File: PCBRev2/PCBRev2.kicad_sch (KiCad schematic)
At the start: 55 parts, among them J1 Conn_02x40_Counter_Clockwise, J3 512964594, J5 Keypad, J6 Conn_02x10_Odd_Even, J7 54-00164, Q1 2N7000, SW1 SW_Push, SW2 SW_Push, SW3 SW_Push, U1 NUCLEO-G0B1RE, U10 BH1750FVI-TR, U11 MCP6002-I_P, U12 DRV8833PWP, U2 LP-MSPM0G3507, U4 SN74AHC14N, U5 LM7805_TO220, U6 TLV1117-33, U7 COM-09032, U8 WST-1205S, U9 AL5809-20QP1-7

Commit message: Routing for second revision of the PCB
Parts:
- removed C_BP3, C_BP4: 100 uf, Capacitor_THT:C_Axial_L3.8mm_D2.6mm_P7.50mm_Horizontal, symbol Device:C_Small
- removed D1: ASMB-MTB1-0A3A2, LED_SMD:LED_Avago_PLCC4_3.2x2.8mm_CW, symbol LED:ASMB-MTB1-0A3A2
- removed J1: Conn_02x40_Counter_Clockwise, Connector_PinHeader_2.54mm:PinHeader_2x40_P2.54mm_Vertical, symbol Connector_Generic:Conn_02x40_Counter_Clockwise
- removed R_BUZ2: 100kR, Resistor_THT:R_Axial_DIN0207_L6.3mm_D2.5mm_P5.08mm_Vertical, symbol Device:R
- removed U8: WST-1205S, WST-1205S.step:WST-1205S, symbol WST-1205S:WST-1205S
- added C10: 0.22uf, GRM155R71C224KA12D022uf.step:CAPC1005X55N, symbol Device:C_Small
- added C11: 1uf, CL03A105KP3NSNC1uf.step:CAPC0603X35N, symbol Device:C_Small
- added D2: AAAF3529LSEEZGKQBKS, LED_AAAF3529LSEEZGKQBKS_KNB, symbol 2025-11-19_19-46-32:AAAF3529LSEEZGKQBKS
- added D3, D4, D5: LED, LED_THT:LED_D3.0mm_FlatTop, symbol Device:LED
- added J6: Conn_02x30_Odd_Even, Connector_PinHeader_2.54mm:PinHeader_2x30_P2.54mm_Vertical, symbol Connector_Generic:Conn_02x30_Odd_Even
- added R19, R20: 68, CRGCQ1206F68R.step:RESC3115X65N, symbol Device:R
- added R21: 330, CRCW1210330RFKEAHP.step:RESC3225X70N, symbol Device:R
- added U9: WST-1205S, WST-1205S.step:WST-1205S, symbol WST-1205S:WST-1205S
- C1: renamed from C_BP1; value 0.1 uf -> 0.1uf; footprint Capacitor_THT:C_Axial_L3.8mm_D2.6mm_P7.50mm_Horizontal -> C01UF.step:CAPC1608X90
- C2: renamed from C_BP2; value 47 uf -> 47uf; footprint Capacitor_THT:C_Radial_D10.0mm_H20.0mm_P5.00mm -> GRM32EC81C476KE15L.step:CAPC3225X270N
- C3: renamed from CSW1; footprint Capacitor_THT:C_Axial_L3.8mm_D2.6mm_P7.50mm_Horizontal -> GRM033R60J474KE90D.step:CAPC0603X33N
- C4: renamed from CSW3; footprint Capacitor_THT:C_Axial_L3.8mm_D2.6mm_P7.50mm_Horizontal -> GRM033R60J474KE90D.step:CAPC0603X33N
- C5: renamed from CJS1; footprint Capacitor_THT:C_Axial_L3.8mm_D2.6mm_P7.50mm_Horizontal -> GRM033R60J474KE90D.step:CAPC0603X33N
- C6: renamed from C_s2; footprint Capacitor_THT:C_Axial_L3.8mm_D2.6mm_P7.50mm_Horizontal -> CL03A105KP3NSNC1uf.step:CAPC0603X35N
- Q1: value 2N7000 -> 2N4401
- R1: renamed from PullUpResistorSW1; footprint Resistor_THT:R_Axial_DIN0207_L6.3mm_D2.5mm_P5.08mm_Vertical -> RC0603FR_0710KL.step:RESC1607X60N
- R10: renamed from R_SNSA2; footprint Resistor_THT:R_Axial_DIN0207_L6.3mm_D2.5mm_P5.08mm_Vertical -> CRGCQ0603F2K2.step:RESC1608X55N
- R11: renamed from R_SNSA3; footprint Resistor_THT:R_Axial_DIN0207_L6.3mm_D2.5mm_P5.08mm_Vertical -> CRGCQ0603F2K2.step:RESC1608X55N
- R12: renamed from R_SNSA5; footprint Resistor_THT:R_Axial_DIN0207_L6.3mm_D2.5mm_P5.08mm_Vertical -> CRGCQ0603F2K2.step:RESC1608X55N
- R13: renamed from R_SNSA6; footprint Resistor_THT:R_Axial_DIN0207_L6.3mm_D2.5mm_P5.08mm_Vertical -> CRGCQ0603F2K2.step:RESC1608X55N
- R14: renamed from R_SNSA4; value 70kR -> 68k; footprint Resistor_THT:R_Axial_DIN0207_L6.3mm_D2.5mm_P5.08mm_Vertical -> CRGP2512F68K.step:RESC6332X65N
- R15: renamed from R_BUZ1; value 100R -> 1kR
- R16: renamed from PullUpResistor2; footprint Resistor_THT:R_Axial_DIN0207_L6.3mm_D2.5mm_P5.08mm_Vertical -> RC0603FR_0710KL.step:RESC1607X60N
- R18: renamed from R_INDC1; value 5.5k ohm -> 510; footprint Resistor_THT:R_Axial_DIN0207_L6.3mm_D2.5mm_P5.08mm_Vertical -> RMCF0805JT510R510.step:RESC2012X65N
- R2: renamed from RSW1; footprint Resistor_THT:R_Axial_DIN0207_L6.3mm_D2.5mm_P5.08mm_Vertical -> RC0603FR_0710KL.step:RESC1607X60N
- R3: renamed from PullUpResistorSW3; footprint Resistor_THT:R_Axial_DIN0207_L6.3mm_D2.5mm_P5.08mm_Vertical -> RC0603FR_0710KL.step:RESC1607X60N
- R4: renamed from RSW3; footprint Resistor_THT:R_Axial_DIN0207_L6.3mm_D2.5mm_P5.08mm_Vertical -> RC0603FR_0710KL.step:RESC1607X60N
- R5: renamed from PullUpResistorJS1; footprint Resistor_THT:R_Axial_DIN0207_L6.3mm_D2.5mm_P5.08mm_Vertical -> RC0603FR_0710KL.step:RESC1607X60N
- R6: renamed from RJS1; footprint Resistor_THT:R_Axial_DIN0207_L6.3mm_D2.5mm_P5.08mm_Vertical -> RC0603FR_0710KL.step:RESC1607X60N
- R7: renamed from R_COFF2; footprint Resistor_THT:R_Axial_DIN0207_L6.3mm_D2.5mm_P5.08mm_Vertical -> RNCP1206FTD1K00.step:RESC3216X90N
- R8: renamed from R_COFF3; footprint Resistor_THT:R_Axial_DIN0207_L6.3mm_D2.5mm_P5.08mm_Vertical -> RNCP1206FTD1K00.step:RESC3216X90N
- R9: renamed from R_COFF4; footprint Resistor_THT:R_Axial_DIN0207_L6.3mm_D2.5mm_P5.08mm_Vertical -> RNCP1206FTD1K00.step:RESC3216X90N
- U7: renamed from U4; footprint Schmitt:DIP794W45P254L1969H508Q14 -> SN74AHCT14QDRG4Q1.step:SOIC127P600X175-14N
- renumbered C3 to C7, C2 to C8, C1 to C9, D2 to D1, J7 to J1, J6 to J2, J10 to J3, J5 to J4, J4 to J5, J3 to J8, R10 to R17, SW3 to SW2, SW2 to SW3, U9 to U10, U5 to U2, U6 to U3, U2 to U4, U7 to U5, U12 to U6, U10 to U8
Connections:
- net +12V: now also C10.1
- net +5V: now also U9.+; no longer Q1.3 (D)
- net BuzzerGPIO: now also J6.10 (Pin_10), J6.9 (Pin_9)
- net GNDREF: now also Q1.1 (S), C10.2, C11.2, D2.1, D2.2, D2.3, D3.1 (K), D4.1 (K), D5.1 (K)
- net MicOut: now also J6.27 (Pin_27), J6.28 (Pin_28)
- net MotorControl1: now also J6.1 (Pin_1), J6.2 (Pin_2)
- net MotorControl2: now also J6.5 (Pin_5), J6.6 (Pin_6)
- net Motor_Sleep: now also J6.3 (Pin_3), J6.4 (Pin_4)
- net VDD: now also C11.1
- net G: now reaches R8.1
- net G: now also J6.39 (Pin_39), J6.40 (Pin_40)
- net at R8.2: now also D2.5
- net B: now reaches R7.1
- net B: now also J6.37 (Pin_37), J6.38 (Pin_38)
- net at R7.2: now also D2.4
- net H: now reaches U5.H2 (H)
- net H: now also J6.23 (Pin_23), J6.24 (Pin_24)
- net V: now reaches U5.V2 (V)
- net V: now also J6.21 (Pin_21), J6.22 (Pin_22)
- net SDA: now reaches U8.4 (SDA)
- net SDA: now also J6.31 (Pin_31), J6.32 (Pin_32)
- net SCLlight: now reaches U8.6 (SCL)
- net SCLlight: now also J6.33 (Pin_33), J6.34 (Pin_34)
- net SW1: now reaches U7.2 (1Y)
- net SW1: now also J6.13 (Pin_13), J6.14 (Pin_14), R19.1
- net SW2: now reaches U7.4 (2Y)
- net SW2: now also J6.15 (Pin_15), J6.16 (Pin_16), R20.1
- net JSB: now reaches U7.6 (3Y)
- net JSB: now also J6.17 (Pin_17), J6.18 (Pin_18), R21.1
- net SDO: now reaches J8.29
- net SDO: now also J6.51 (Pin_51), J6.52 (Pin_52)
- net SDI: now reaches J8.30
- net SDI: now also J6.53 (Pin_53), J6.54 (Pin_54)
- net SCL: now reaches J8.32
- net SCL: now also J6.55 (Pin_55), J6.56 (Pin_56)
- net D/CX: now reaches J8.33
- net D/CX: now also J6.57 (Pin_57), J6.58 (Pin_58)
- net CSX: now reaches J8.34
- net CSX: now also J6.59 (Pin_59), J6.60 (Pin_60)
- net RESX: now reaches J8.6
- net RESX: now also J6.49 (Pin_49), J6.50 (Pin_50)
- net R: now reaches R9.1
- net R: now also J6.41 (Pin_41), J6.42 (Pin_42)
- net at R9.2: now also D2.6
- net Button No Debouning renamed ButtonNoDebounce
- net ButtonNoDebounce: now also J6.45 (Pin_45), J6.46 (Pin_46)
- new net: D3.2 (A), R19.2
- new net: J6.11 (Pin_11), J6.12 (Pin_12)
- new net: J6.19 (Pin_19), J6.20 (Pin_20)
- new net: J6.25 (Pin_25), J6.26 (Pin_26)
- new net: J6.29 (Pin_29), J6.30 (Pin_30)
- new net: J6.35 (Pin_35), J6.36 (Pin_36)
- new net: J6.43 (Pin_43), J6.44 (Pin_44)
- new net: J6.47 (Pin_47), J6.48 (Pin_48)
- new net: J6.7 (Pin_7), J6.8 (Pin_8)
- new net: Q1.3 (D), U9.-
- new net: D4.2 (A), R20.2
- new net: D5.2 (A), R21.2
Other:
- moved on the sheet: R16, R7, R8, R9, SW3, U8

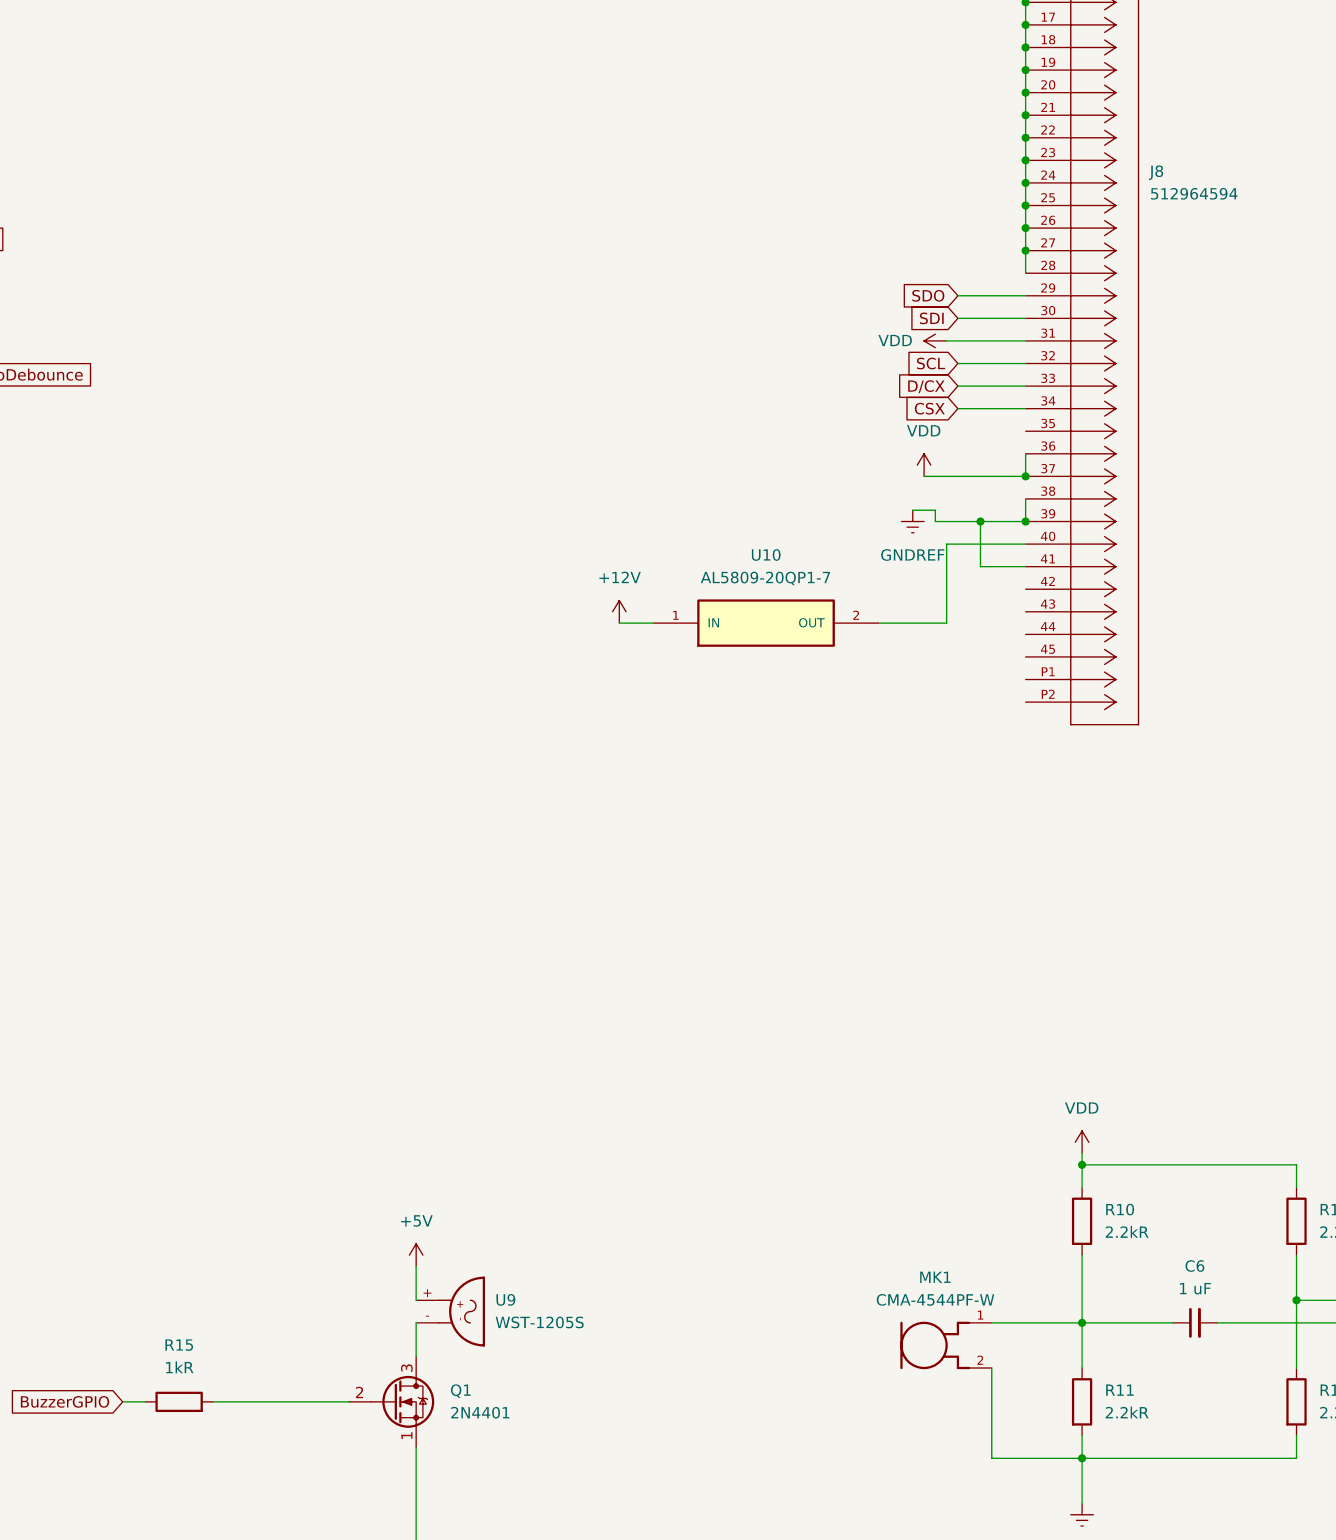
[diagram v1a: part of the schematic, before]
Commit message: Updated routing and footprints for 2nd PCB revision
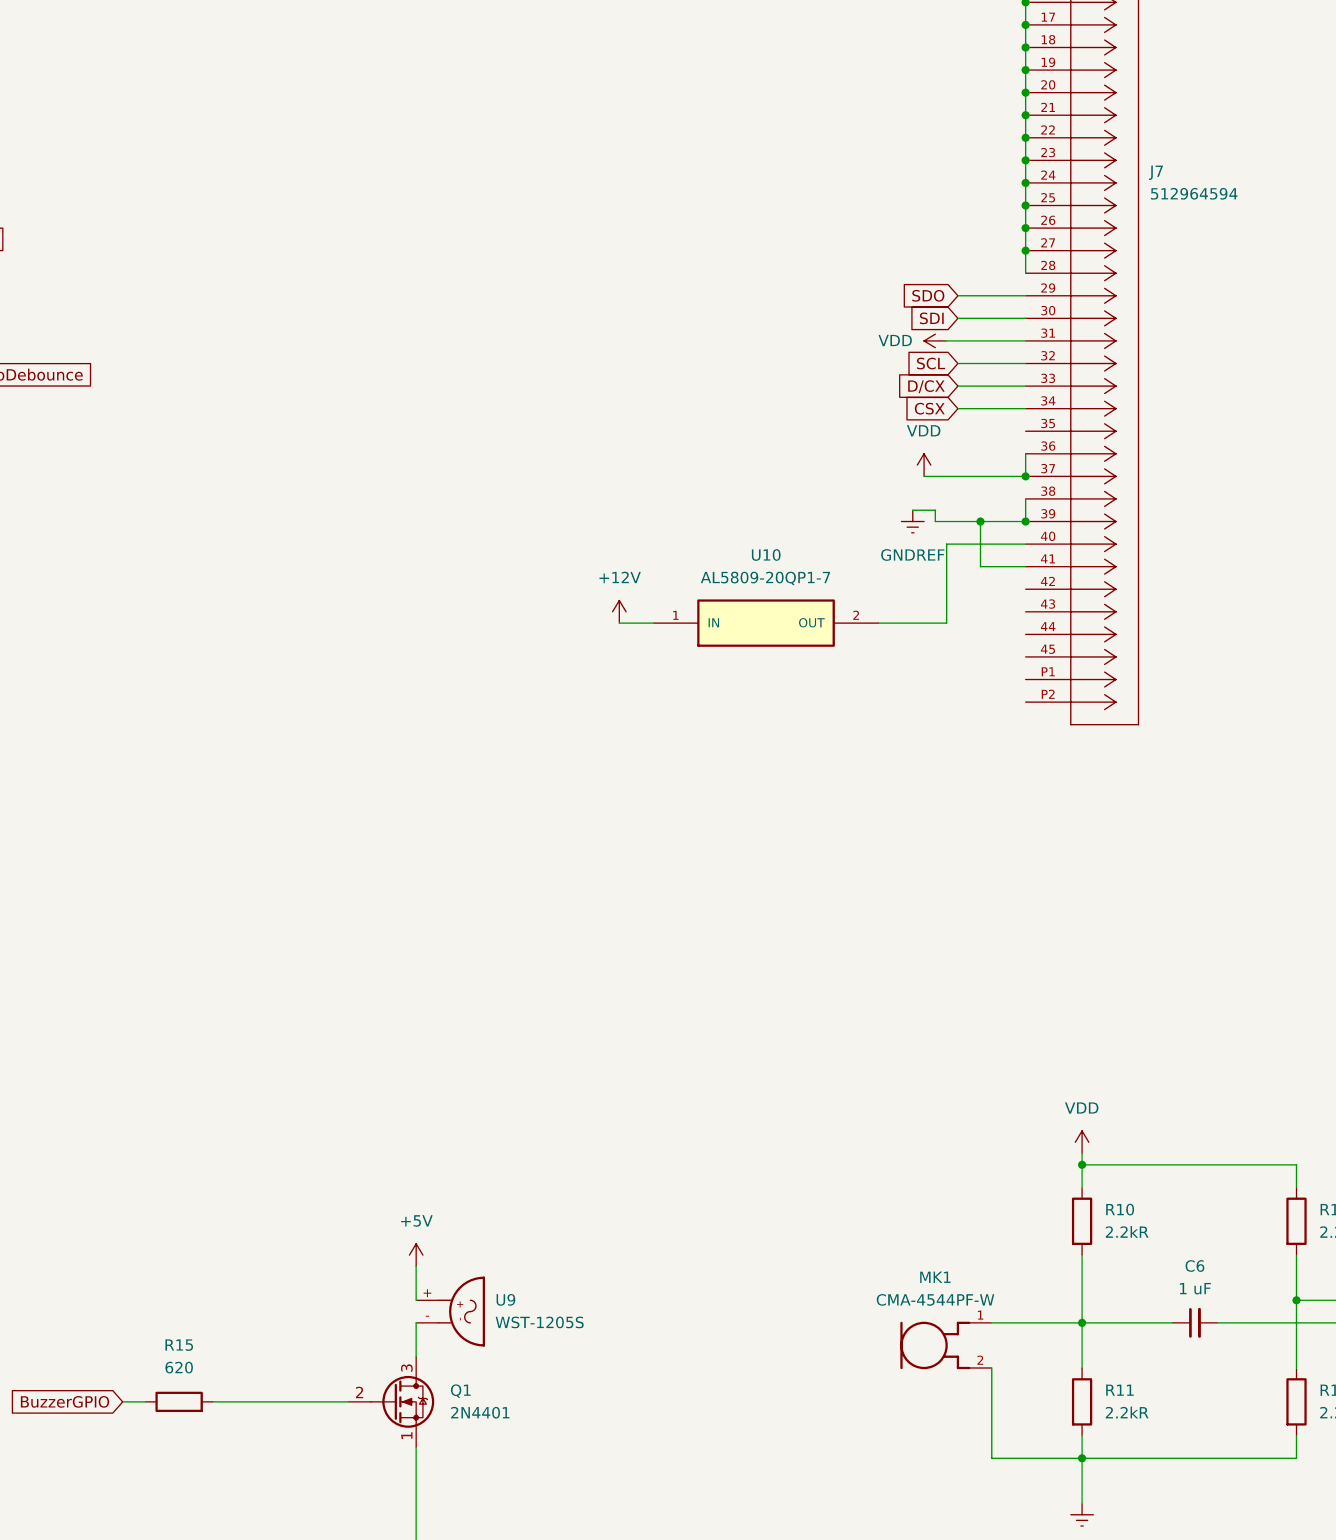
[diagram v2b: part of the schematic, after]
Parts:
- J6: footprint Connector_PinHeader_2.54mm:PinHeader_2x30_P2.54mm_Vertical -> Connector_PinHeader_2.54mm:PinHeader_2x32_P2.54mm_Vertical
- R15: value 1kR -> 620; footprint Resistor_THT:R_Axial_DIN0207_L6.3mm_D2.5mm_P5.08mm_Vertical -> RC1206JR_07620RL.step:RESC3116X65N
- renumbered J8 to J7
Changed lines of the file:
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@@
 			)
 		)
-		(property "Footprint" "Connector_PinHeader_2.54mm:PinHeader_2x30_P2.54mm_Vertical"
+		(property "Footprint" "Connector_PinHeader_2.54mm:PinHeader_2x32_P2.54mm_Vertical"
 			(at 303.53 76.2 0)
 			(effects
@@
 			)
 		)
-		(property "Value" "1kR"
+		(property "Value" "620"
 			(at 340.36 208.28 90)
 			(effects
@@
 			)
 		)
-		(property "Footprint" "Resistor_THT:R_Axial_DIN0207_L6.3mm_D2.5mm_P5.08mm_Vertical"
+		(property "Footprint" "RC1206JR_07620RL.step:RESC3116X65N"
 			(at 340.36 213.868 90)
 			(effects
@@
 		(dnp no)
 		(fields_autoplaced yes)
-		(property "Reference" "J8"
+		(property "Reference" "J7"
 			(at 449.58 73.6599 0)
 			(effects
@@
 			(project ""
 				(path "/39e7582f-7765-4fc9-b934-76d5b28d9065"
-					(reference "J8")
+					(reference "J7")
 					(unit 1)
 				)

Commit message: Updated silkscreen
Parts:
- added J10: 3.3V, Connector_PinHeader_2.54mm:PinHeader_1x01_P2.54mm_Vertical, symbol Connector:Conn_01x01_Pin
- added J8: 12V, Connector_PinHeader_2.54mm:PinHeader_1x01_P2.54mm_Vertical, symbol Connector:Conn_01x01_Pin
- added J9: 5V, Connector_PinHeader_2.54mm:PinHeader_1x01_P2.54mm_Vertical, symbol Connector:Conn_01x01_Pin
- C1: footprint C01UF.step:CAPC1608X90 -> Capacitor_SMD:C_0603_1608Metric
- C10: footprint GRM155R71C224KA12D022uf.step:CAPC1005X55N -> Capacitor_SMD:C_0603_1608Metric
- C11, C6: footprint CL03A105KP3NSNC1uf.step:CAPC0603X35N -> Capacitor_SMD:C_0603_1608Metric
- C2: footprint GRM32EC81C476KE15L.step:CAPC3225X270N -> Capacitor_SMD:C_1210_3225Metric_Pad1.33x2.70mm_HandSolder
- C3, C4, C5: footprint GRM033R60J474KE90D.step:CAPC0603X33N -> Capacitor_SMD:C_0603_1608Metric
- R1, R16, R2, R3, R4, R5, R6: footprint RC0603FR_0710KL.step:RESC1607X60N -> Resistor_SMD:R_0603_1608Metric
- R10, R11, R12, R13: footprint CRGCQ0603F2K2.step:RESC1608X55N -> Resistor_SMD:R_0603_1608Metric
- R14: footprint CRGP2512F68K.step:RESC6332X65N -> Resistor_SMD:R_0603_1608Metric
- R15: footprint RC1206JR_07620RL.step:RESC3116X65N -> Resistor_SMD:R_0603_1608Metric
- R18: footprint RMCF0805JT510R510.step:RESC2012X65N -> Resistor_SMD:R_0603_1608Metric
- R19, R20: footprint CRGCQ1206F68R.step:RESC3115X65N -> Resistor_SMD:R_0603_1608Metric
- R21: footprint CRCW1210330RFKEAHP.step:RESC3225X70N -> Resistor_SMD:R_0603_1608Metric
- R7, R8: value 1kR -> 300; footprint RNCP1206FTD1K00.step:RESC3216X90N -> Resistor_SMD:R_0603_1608Metric
- R9: value 1kR -> 750; footprint RNCP1206FTD1K00.step:RESC3216X90N -> Resistor_SMD:R_0603_1608Metric
- U7: value SN74AHC14N -> SN74AHCT14QDRG4Q1
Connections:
- net +12V: now also J8.1 (Pin_1)
- net +5V: now also J9.1 (Pin_1)
- net VDD: now also J10.1 (Pin_1)
- net +3.3V: no longer names the net of U1.CN6_2 (3V3), U1.CN6_4 (3V3), U1.CN7_12 (3V3), U1.CN7_16 (3V3), U1.JP3_2 (3V3)
